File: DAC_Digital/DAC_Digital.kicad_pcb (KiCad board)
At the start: 2 copper layers, 100 x 100 mm, 120 parts, among them J1 +5V_in, J10 USB_Dev4, J11 P9, J12 Anlg_in, J13 Anlg_in, J14 P8, J2 DBG_PORT, J3 DSPL_PORT, J4 Conn_01x02, J5 USB0, J6 USB1, J7 USB_Dev1, J8 USB_Dev2, J9 USB_Dev3, Q1 2n7002, Q2 2N7002, Q3 FDS4435, Q4 FDS4435, Q5 2N7002, Q6 2N7002, T1 DA103C, U1 CS8406_2, U2 PIC18F6722, U3 74LVC1G08GW, U4 PCM2903C, U5 74LVC1G08GW, U6 USB2514B-AEZC, U7 NE5532, X1 7A-24.000MAAJ-T, Y1 10MHz, Y2 12MHz

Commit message: Update IACSense footprint
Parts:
- added J15: Test, Pin_Headers:Pin_Header_Straight_1x08_Pitch1.00mm, F.Cu at (131.0, 151.0)
- added J16: Test, Pin_Headers:Pin_Header_Straight_1x08_Pitch1.00mm, F.Cu at (145.0, 149.0)
- J13: value Anlg_in -> Anlg_I2C

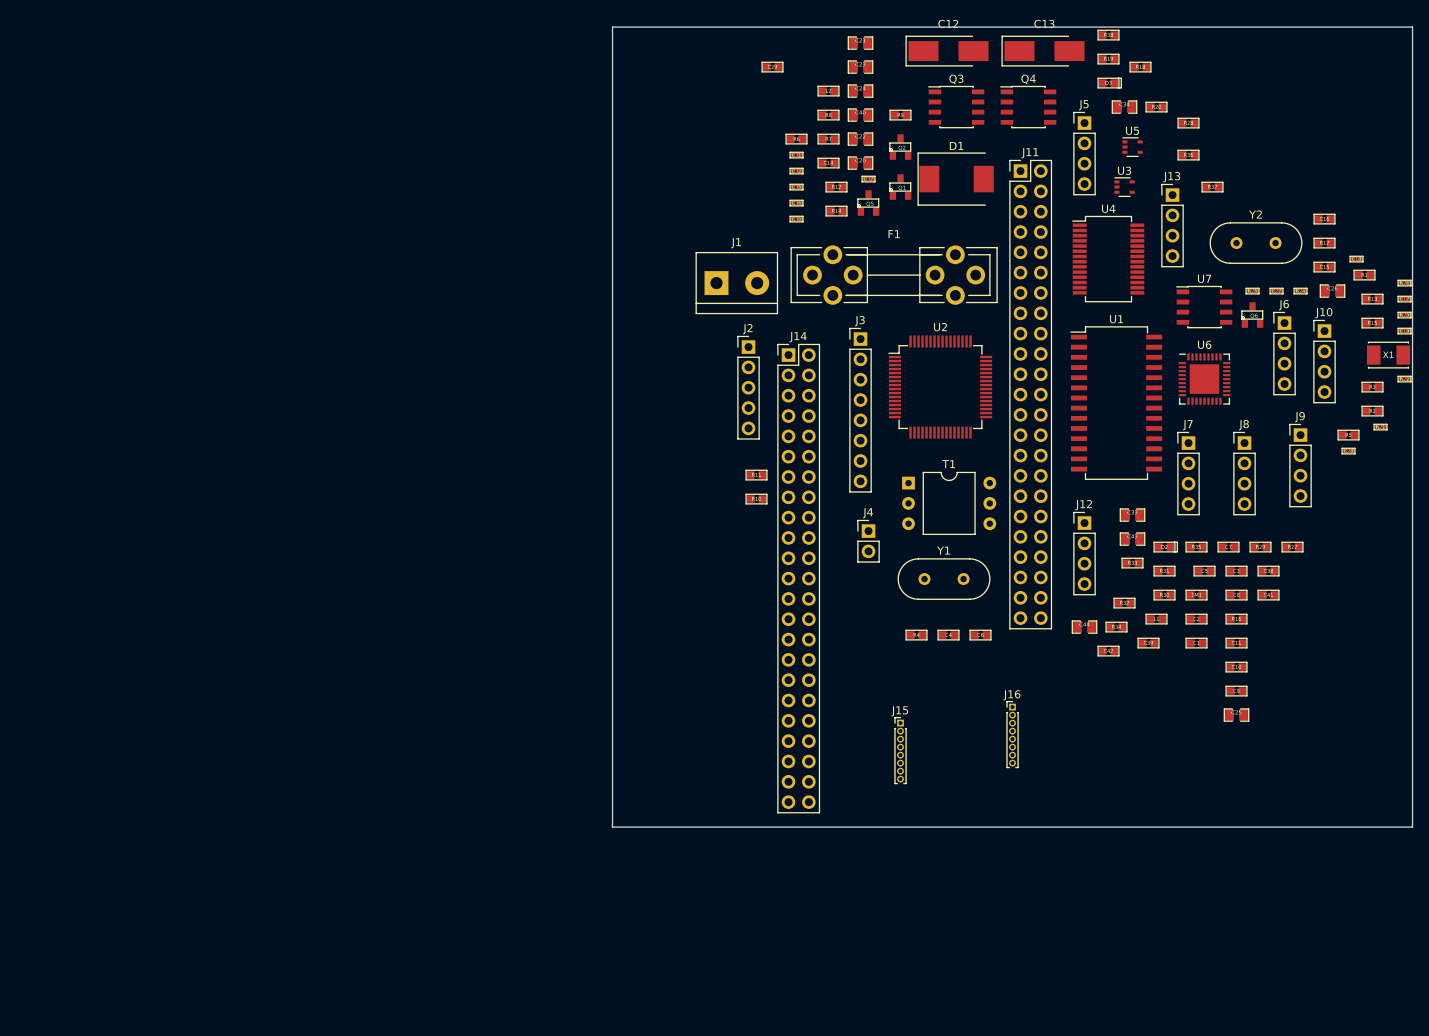
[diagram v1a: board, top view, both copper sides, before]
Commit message: place all components on DAC_Analog
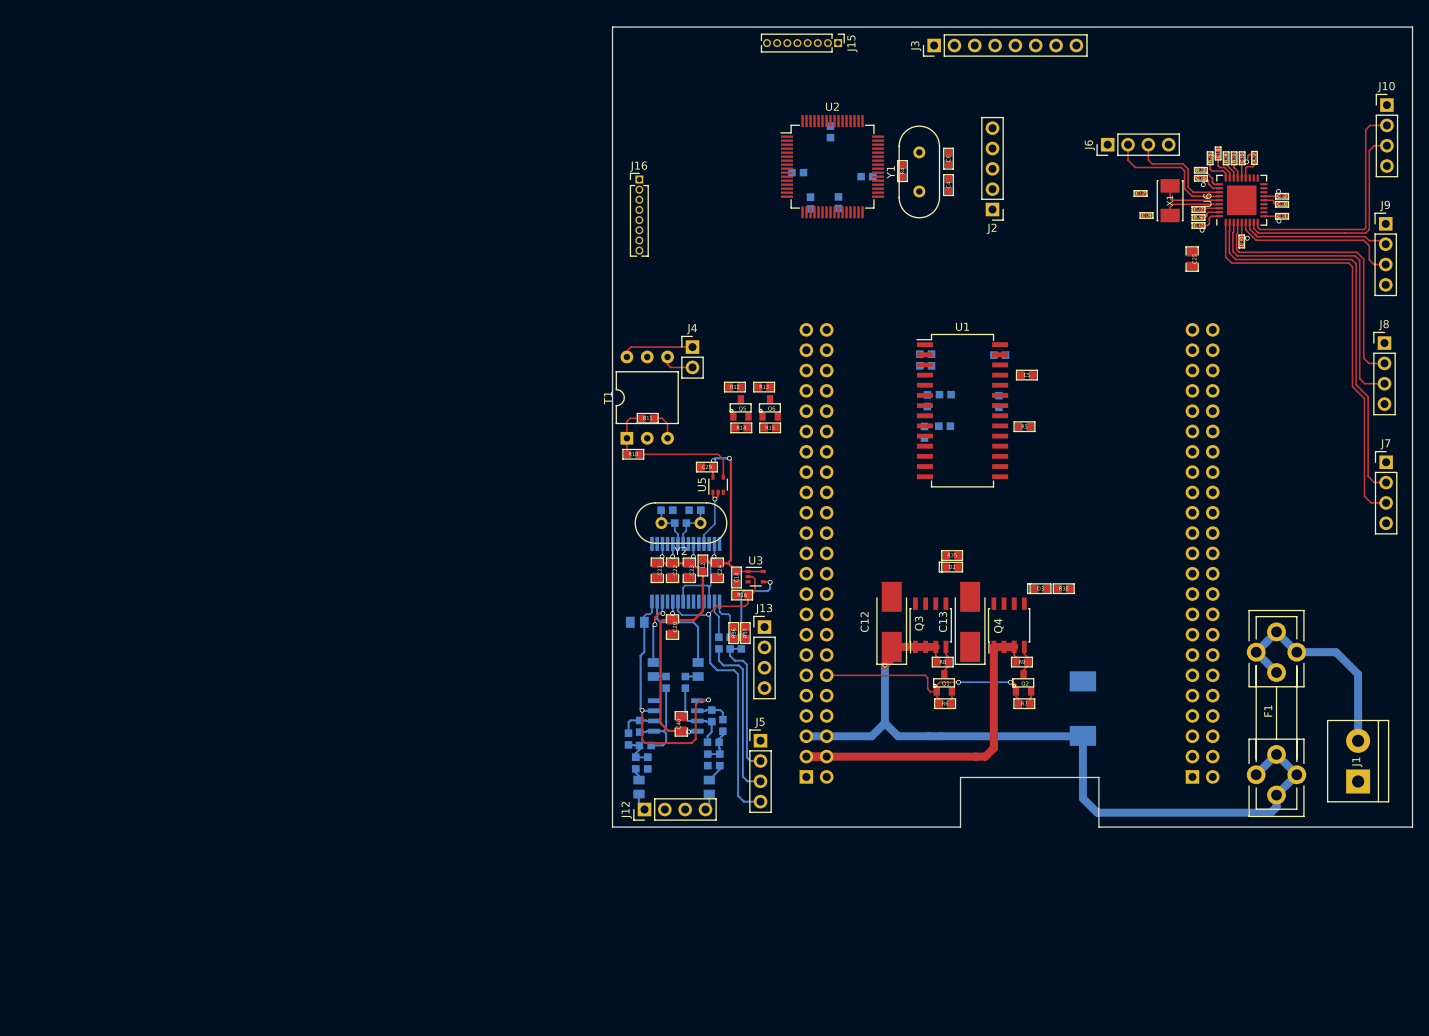
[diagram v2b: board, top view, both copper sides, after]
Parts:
- removed 1M1: R, Yame_library:SM0603-MR
- added R39: 1meg, Yame_library:SM0603-MR, B.Cu at (136.5, 113.9)
- C1, C10, C11, C15, C16, C2, C26, C3, C33, C34, C38, C39, C41, C42, C43, C44, C7, C8, C9, D1, J11, J14, L1, R1, R17, R18, R19, R2, R20, R27, R28, R29, R3, R30, R31, R32, R33, R34, U4, U7: moved to B.Cu
- J15, J16: footprint Pin_Headers:Pin_Header_Straight_1x08_Pitch1.00mm -> Pin_Headers:Pin_Header_Straight_1x08_Pitch1.27mm
- J4: value Conn_01x02 -> Out_SPDIF
- moved J1 101.6 mm to (188.2, 158.3), turned to 90 degrees
- moved C26 96.3 mm to (98.1, 138.4)
- moved R28 94.0 mm to (104.1, 145.9), turned to 90 degrees
- moved C16 89.9 mm to (101.8, 124.4)
- moved C34 88.2 mm to (105.7, 144.3), turned to 90 degrees
- moved R17 87.8 mm to (103.5, 126.0)
- moved R18 87.6 mm to (111.1, 141.0), turned to 270 degrees
- moved J5 87.2 mm to (113.5, 153.2)
- moved R19 87.0 mm to (109.7, 141.0), turned to 270 degrees
- moved R20 86.5 mm to (108.3, 141.0), turned to 270 degrees
- moved J15 85.4 mm to (123.2, 66.0), turned to 270 degrees
- moved C15 84.4 mm to (105.3, 124.4), turned to 180 degrees
- moved U7 83.5 mm to (102.9, 150.1)
- moved R36 82.5 mm to (110.2, 139.8), turned to 270 degrees
- moved C11 81.6 mm to (122.2, 77.1), turned to 270 degrees
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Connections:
- C20 pad 1: VCC -> /Vanlg
- C21 pad 1: VCC -> /Vanlg
- C22 pad 1: VCC -> /Vanlg
- C23 pad 1: VCC -> /Vanlg
- C25 pad 1: +3.3V -> VCC
- C40 pad 1: VCC -> /Vanlg
- L2 pad 1: VCC -> /Vanlg
- U1 pad 23: Net-(U1-Pad23) -> /+5v_Dev
- U4 pad 10: VCC -> /Vanlg
- U4 pad 17: VCC -> /Vanlg
- U4 pad 19: VCC -> /Vanlg
- U4 pad 23: VCC -> /Vanlg
- U7 pad 8: VCC -> /Vanlg
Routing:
- net /VDD_5V: track 0.00 -> 98.6 mm, vias 0 -> 1
- net VCC: track 0.00 -> 62.2 mm, vias 0 -> 9
- net /D-_Dev1: track 0.00 -> 53.0 mm
- net /D+_Dev1: track 0.00 -> 50.0 mm
- net /VDD_3V3B: track 0.00 -> 44.9 mm
- net /Vanlg: track 0.00 -> 44.7 mm, vias 0 -> 5
- net /+5v_Dev: track 0.00 -> 43.9 mm, vias 0 -> 1
- net /D-_Dev2: track 0.00 -> 38.1 mm
- net /D+_Dev2: track 0.00 -> 35.1 mm
- net /Vcom: track 0.00 -> 34.4 mm, vias 0 -> 2
- net /GPIO_60: track 0.00 -> 30.5 mm, vias 0 -> 2
- net /D+_Dev4: track 0.00 -> 29.4 mm
- net /D-_Dev4: track 0.00 -> 27.9 mm
- net Net-(F1-Pad1): track 0.00 -> 27.9 mm
- net /D-_Dev3: track 0.00 -> 21.2 mm
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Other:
- outline, holes or cut-outs redrawn
- net class Default: trace_width 0.25 -> 0.2

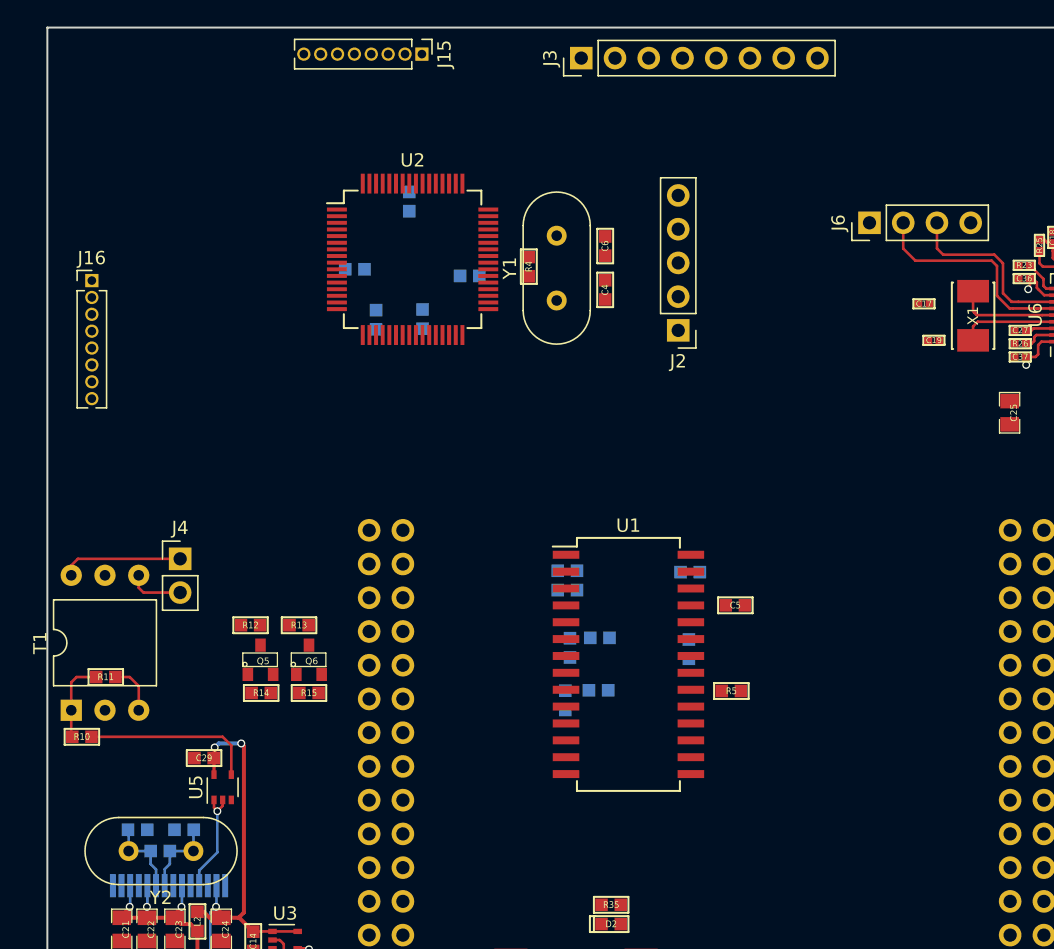
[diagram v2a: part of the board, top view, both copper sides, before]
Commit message: update layout DAC_Digital
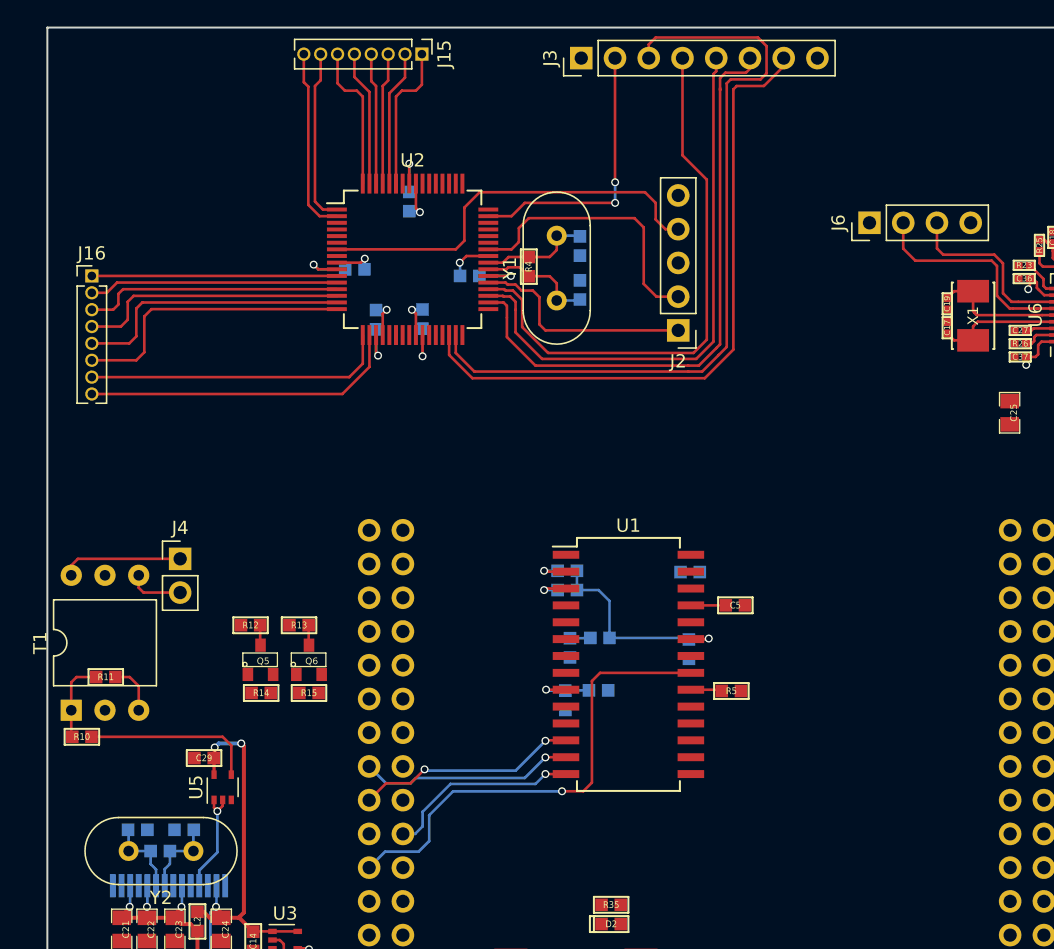
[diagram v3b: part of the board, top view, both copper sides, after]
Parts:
- C4, C6: moved to B.Cu
- moved C19 2.93 mm to (162.8, 84.8), turned to 270 degrees
- moved C17 2.51 mm to (162.8, 86.6), turned to 90 degrees
- moved C4 1.90 mm to (135.1, 83.8)
- moved C6 1.90 mm to (135.1, 80.5)
- moved J16 0.35 mm to (98.3, 82.7)
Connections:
- J13 pad 1: /VDD_3V3B -> VCC
- J6 pad 4: /VDD_5V -> /VDD_5V_USB1
- R36 pad 1: /VDD_3V3B -> VCC
- R37 pad 1: /VDD_3V3B -> VCC
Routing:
- net Net-(J3-Pad3): track 0.00 -> 58.7 mm
- net Net-(J3-Pad7): track 0.00 -> 49.2 mm
- net Net-(J3-Pad6): track 0.00 -> 45.0 mm
- net Net-(J3-Pad5): track 0.00 -> 42.2 mm
- net Net-(J3-Pad4): track 0.00 -> 42.0 mm
- net /GPIO_117: track 0.00 -> 35.9 mm, vias 0 -> 1
- net /+5v_Dev: track 43.9 -> 79.3 mm, vias 1 -> 7
- net Net-(J2-Pad4): track 0.00 -> 30.8 mm
- net Net-(J16-Pad8): track 0.00 -> 24.1 mm
- net Net-(J16-Pad7): track 0.00 -> 23.0 mm
- net Net-(J16-Pad6): track 0.00 -> 21.6 mm
- net Net-(J16-Pad5): track 0.00 -> 21.0 mm
- net Net-(J3-Pad2): track 0.00 -> 20.9 mm, vias 0 -> 2
- net Net-(J2-Pad2): track 0.00 -> 20.8 mm
- net Net-(J16-Pad4): track 0.00 -> 20.2 mm
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
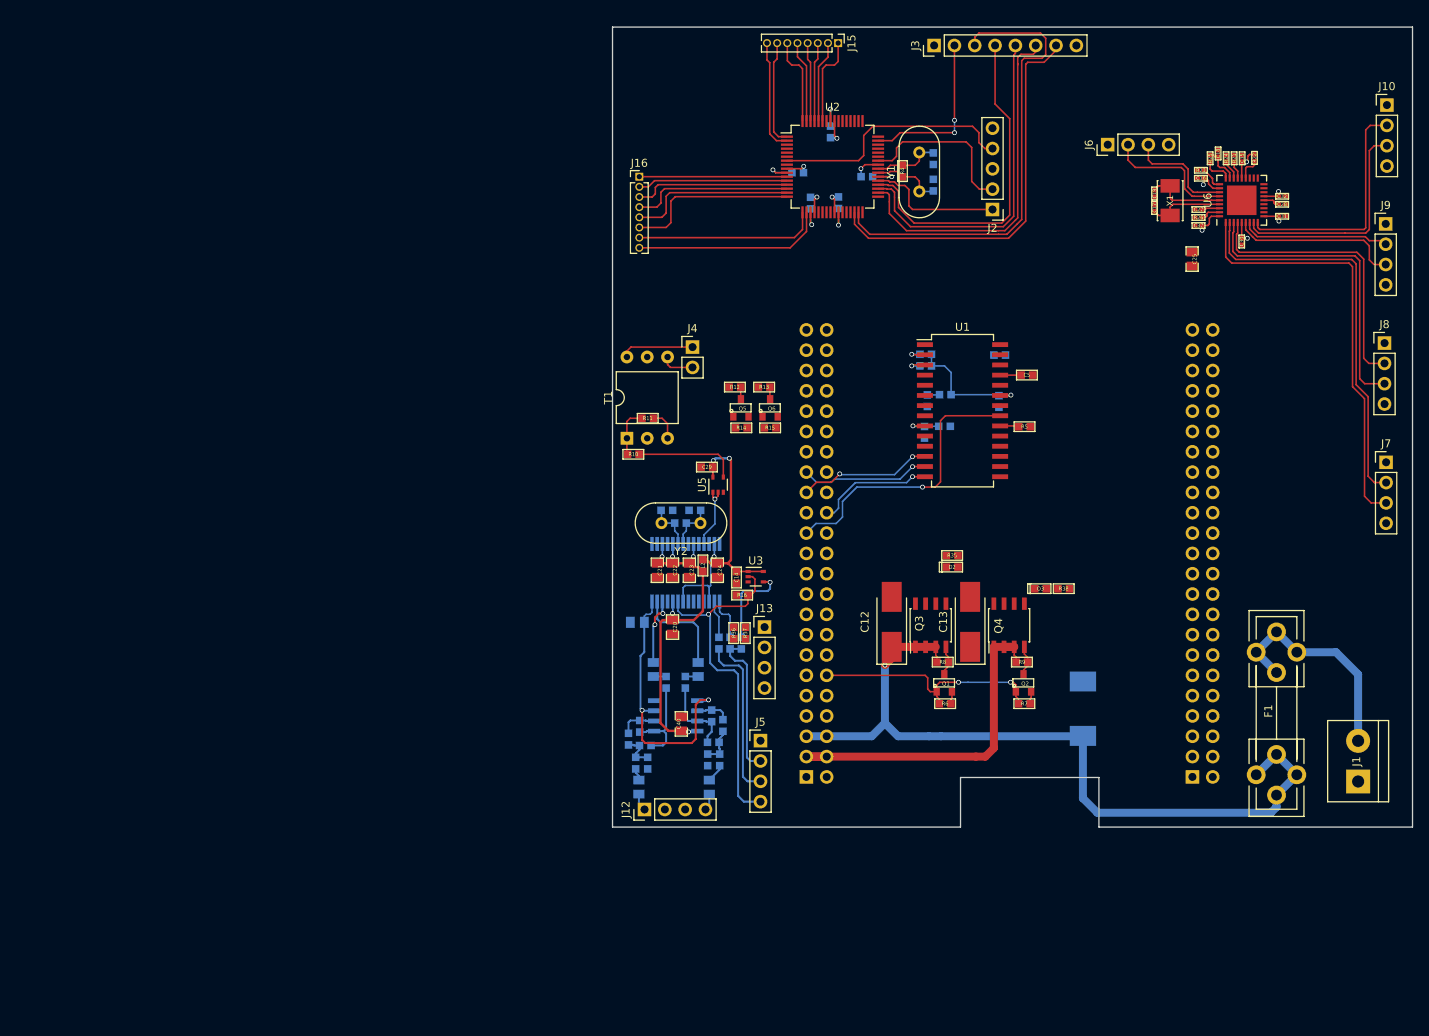
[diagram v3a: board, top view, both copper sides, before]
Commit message: Finish DAC_Digital layout
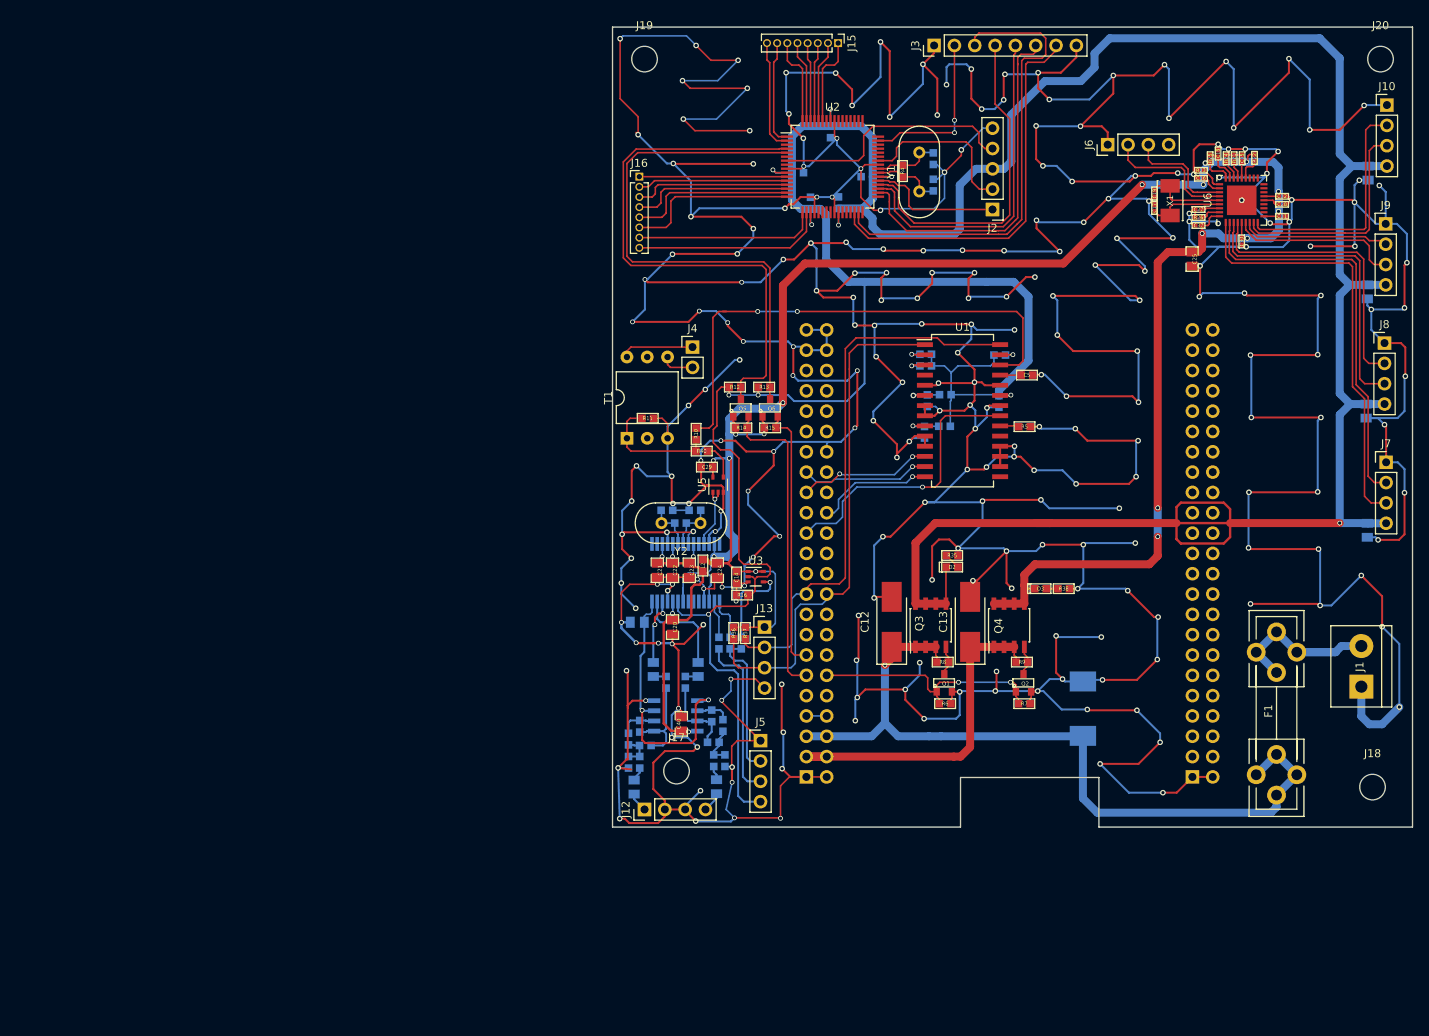
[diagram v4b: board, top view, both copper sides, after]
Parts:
- added C45: 10u, Yame_library:SM0805-MR, B.Cu at (189.3, 126.9)
- added C46: 10u, Yame_library:SM0805-MR, B.Cu at (189.2, 112.0)
- added C47: 10u, Yame_library:SM0805-MR, B.Cu at (189.3, 97.1)
- added C48: 10u, Yame_library:SM0805-MR, B.Cu at (189.4, 82.2)
- added J17: Fix, Mounting_Holes:MountingHole_3.2mm_M3, F.Cu at (103.0, 157.0)
- added J18: Fix, Mounting_Holes:MountingHole_3.2mm_M3, F.Cu at (190.0, 159.0)
- added J19: Fix, Mounting_Holes:MountingHole_3.2mm_M3, F.Cu at (99.0, 68.0)
- added J20: Fix, Mounting_Holes:MountingHole_3.2mm_M3, F.Cu at (191.0, 68.0)
- added R40: 390, Yame_library:SM0603-MR, F.Cu at (106.2, 117.0)
- moved J1 11.9 mm to (188.6, 146.4)
- moved R10 8.25 mm to (105.5, 114.8), turned to 90 degrees
- moved C41 2.40 mm to (97.0, 155.9)
- moved C42 2.15 mm to (109.0, 155.7)
- moved C44 0.90 mm to (108.0, 158.9)
- moved R34 0.76 mm to (107.7, 155.7)
- moved C43 0.60 mm to (97.7, 159.0)
- moved R33 0.51 mm to (98.4, 155.9)
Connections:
- R10 pad 1: Net-(R10-Pad1) -> /SPDIF_OUT
- R10 pad 2: /SPDIF_OUT -> Net-(R10-Pad2)
- R11 pad 2: Net-(R10-Pad1) -> /SPDIF_OUT
- T1 pad 1: Net-(R10-Pad1) -> /SPDIF_OUT
- U1 pad 26: /SPDIF_OUT -> Net-(R10-Pad2)
- U5 pad 4: /SPDIF_OUT -> Net-(R40-Pad2)
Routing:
- net GND: track 22.1 -> 1709.7 mm, vias 5 -> 259
- net /+5v_Dev: track 79.3 -> 495.1 mm, vias 7 -> 10
- net VCC: track 62.2 -> 296.0 mm, vias 9 -> 17
- net /I2C2_SCL: track 0.00 -> 69.6 mm
- net Net-(Q5-Pad3): track 1.51 -> 70.6 mm
- net Net-(Q6-Pad3): track 1.51 -> 67.0 mm
- net /I2C2_SDA: track 0.00 -> 65.4 mm
- net Net-(R10-Pad2): track 0.00 -> 63.9 mm, vias 0 -> 2
- net /UART4_RXD: track 0.00 -> 39.0 mm
- net /UART4_TXD: track 0.00 -> 33.2 mm
- net Net-(R10-Pad1): track 6.17 -> 0.00 mm
- net Net-(R40-Pad2): track 0.00 -> 4.61 mm
- net Net-(F1-Pad1): track 27.9 -> 24.1 mm
- net /VD: track 1.54 -> 4.77 mm, vias 0 -> 1
- net Net-(R2-Pad1): track 0.00 -> 2.55 mm, vias 0 -> 1
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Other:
- net class Default: clearance 0.2 -> 0.16
- rule trace_clearance: 0.2 -> 0.16
